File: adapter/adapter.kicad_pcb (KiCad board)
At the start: 2 copper layers, 16 parts, among them J1 MALE, J11 MALE, J12 FEMALE, J2 FEMALE, J3 USB_C_Receptacle_USB2.0, J5 DTR, U1 FT232RL

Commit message: Set design rules
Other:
- net class Default: clearance 0.2 -> 0.1524; trace_width 0.25 -> 0.1524; via_dia 0.8 -> 0.6; via_drill 0.4 -> 0.3
- rule trace_clearance: 0.2 -> 0.1524
- rule trace_min: 0.2 -> 0.1016
- rule via_min_size: 0.4 -> 0.5
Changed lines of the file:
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@@
   )
   (setup
-    (last_trace_width 0.25)
-    (trace_clearance 0.2)
+    (last_trace_width 0.1524)
+    (trace_clearance 0.1524)
     (zone_clearance 0.508)
     (zone_45_only no)
-    (trace_min 0.2)
-    (via_size 0.8)
-    (via_drill 0.4)
-    (via_min_size 0.4)
+    (trace_min 0.1016)
+    (via_size 0.6)
+    (via_drill 0.3)
+    (via_min_size 0.5)
     (via_min_drill 0.3)
+    (user_via 0.5 0.3)
     (uvia_size 0.3)
     (uvia_drill 0.1)
@@
   (net 30 "Net-(U1-Pad28)")
   (net_class Default "This is the default net class."
-    (clearance 0.2)
-    (trace_width 0.25)
-    (via_dia 0.8)
-    (via_drill 0.4)
+    (clearance 0.1524)
+    (trace_width 0.1524)
+    (via_dia 0.6)
+    (via_drill 0.3)
     (uvia_dia 0.3)
     (uvia_drill 0.1)

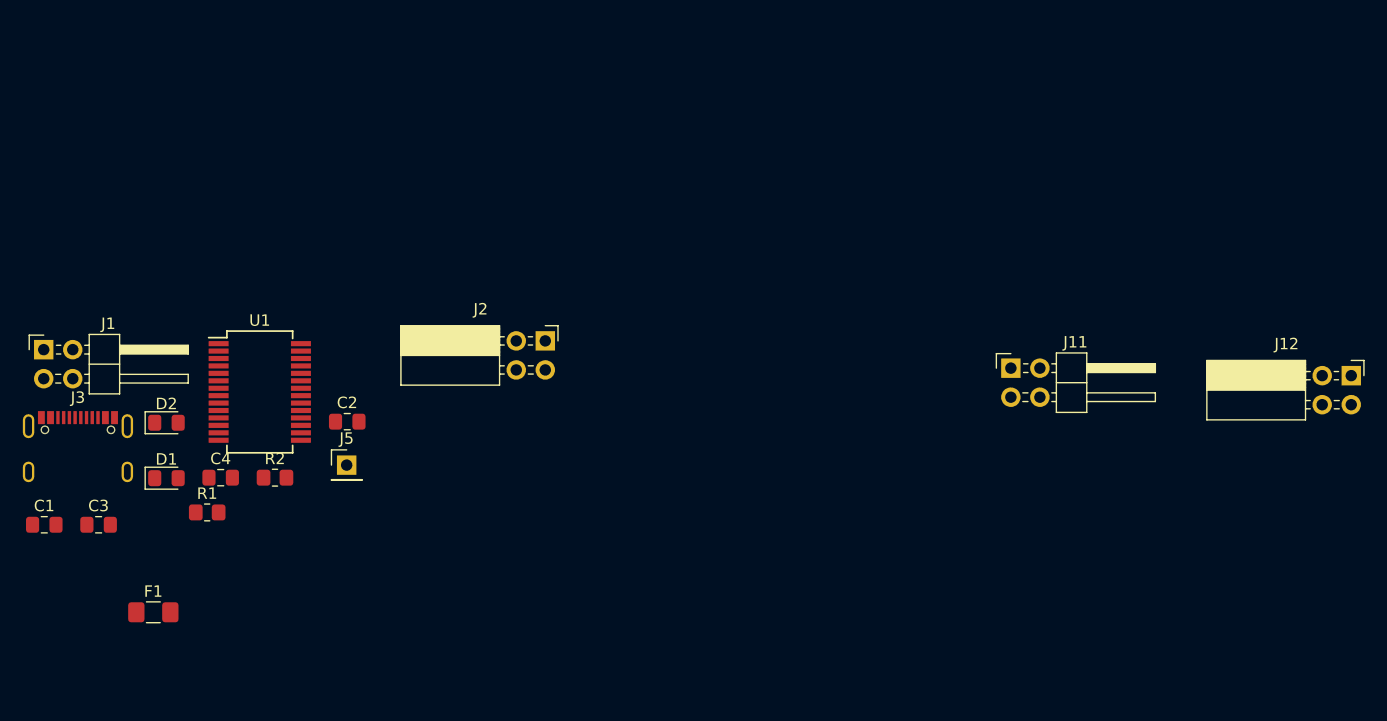
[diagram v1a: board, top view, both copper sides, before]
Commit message: Add holes for standoffs
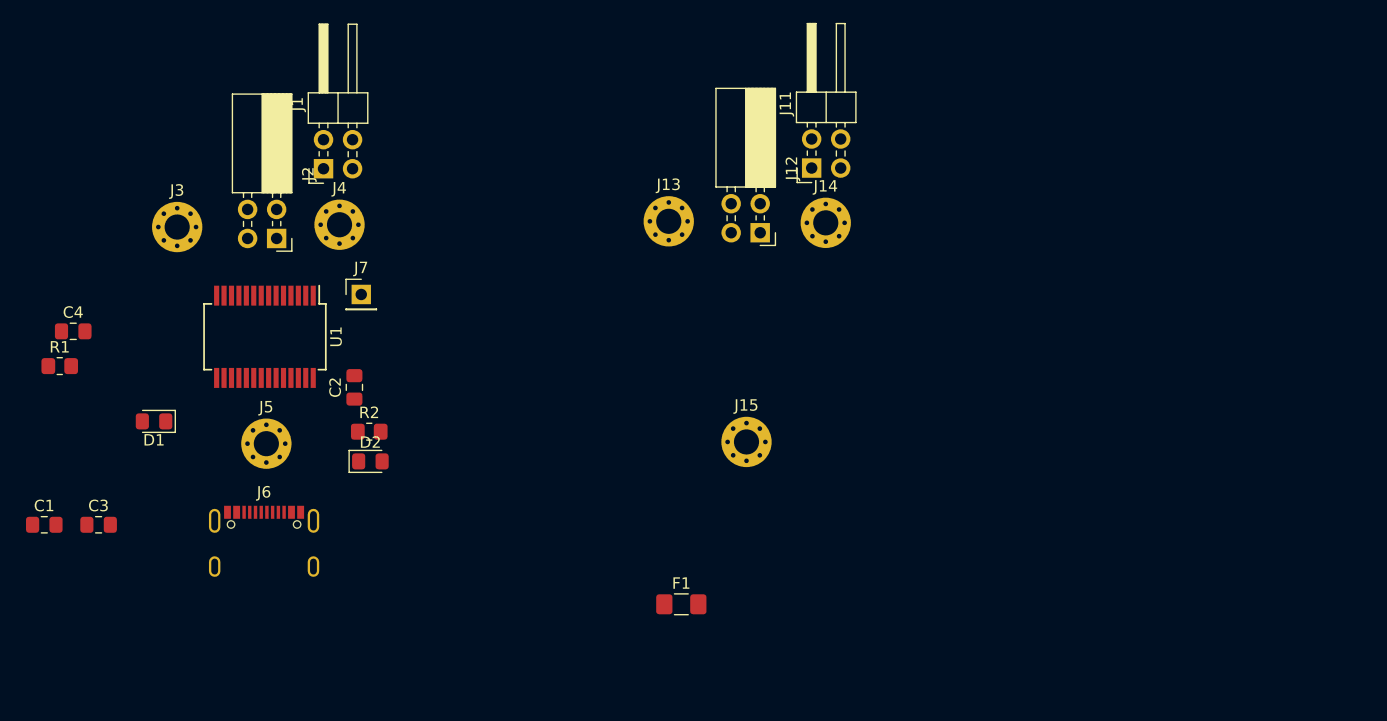
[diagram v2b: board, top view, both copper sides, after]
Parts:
- added J13: Conn_01x01, MountingHole:MountingHole_2.2mm_M2_Pad_Via, F.Cu at (144.0, 73.4)
- added J14: Conn_01x01, MountingHole:MountingHole_2.2mm_M2_Pad_Via, F.Cu at (157.7, 73.5)
- added J15: Conn_01x01, MountingHole:MountingHole_2.2mm_M2_Pad_Via, F.Cu at (150.8, 92.7)
- added J3: Conn_01x01, MountingHole:MountingHole_2.2mm_M2_Pad_Via, F.Cu at (101.0, 73.9)
- added J4: Conn_01x01, MountingHole:MountingHole_2.2mm_M2_Pad_Via, F.Cu at (115.2, 73.7)
- added J5: Conn_01x01, MountingHole:MountingHole_2.2mm_M2_Pad_Via, F.Cu at (108.8, 92.8)
- moved J12 53.2 mm to (152.0, 74.4), turned to 270 degrees
- moved F1 46.2 mm to (145.1, 106.9)
- moved J1 29.1 mm to (113.8, 68.8), turned to 90 degrees
- moved J2 25.2 mm to (109.7, 74.9), turned to 270 degrees
- moved J11 24.7 mm to (156.5, 68.7), turned to 90 degrees
- moved J6 18.3 mm to (108.6, 103.6)
- moved R1 18.2 mm to (90.7, 86.1)
- moved C4 18.2 mm to (91.9, 83.0)
- moved D2 18.2 mm to (117.9, 94.4)
- moved J7 15.0 mm to (117.1, 79.8)
- moved R2 9.18 mm to (117.8, 91.8)
- moved D1 5.09 mm to (99.0, 90.9), turned to 180 degrees
- moved U1 4.85 mm to (108.7, 83.5), turned to 270 degrees
- moved C2 3.06 mm to (116.5, 87.9), turned to 90 degrees
- renumbered J3 to J6, J5 to J7

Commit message: Add edge cuts and roughly place components
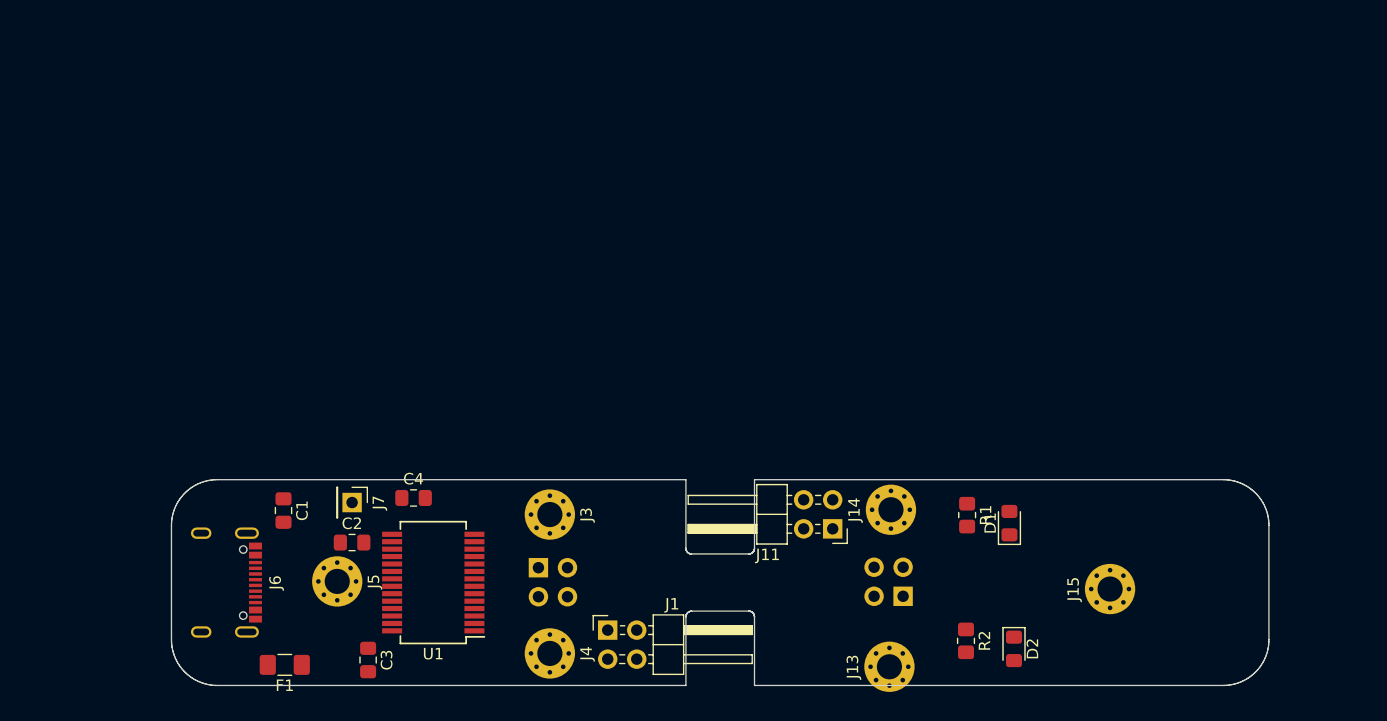
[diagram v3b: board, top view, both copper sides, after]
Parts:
- J12, J2: moved to B.Cu
- moved R1 80.4 mm to (170.1, 99.1), turned to 270 degrees
- moved D1 75.4 mm to (173.8, 99.8), turned to 90 degrees
- moved D2 58.6 mm to (174.2, 110.8), turned to 270 degrees
- moved R2 55.3 mm to (170.0, 110.1), turned to 270 degrees
- moved J1 47.4 mm to (138.7, 109.2), turned to 0 degrees
- moved J13 43.5 mm to (163.3, 112.4), turned to 90 degrees
- moved J4 41.8 mm to (133.6, 111.2), turned to 270 degrees
- moved J3 41.2 mm to (133.6, 99.0), turned to 270 degrees
- moved J2 36.8 mm to (132.6, 103.7), turned to 180 degrees
- moved F1 35.1 mm to (110.4, 112.2), turned to 180 degrees
- moved J15 34.3 mm to (182.6, 105.6), turned to 90 degrees
- moved J12 34.2 mm to (164.5, 106.2), turned to 0 degrees
- moved C4 33.1 mm to (121.7, 97.6)
- moved J11 31.6 mm to (158.3, 100.3), turned to 180 degrees
- moved C3 26.4 mm to (117.7, 111.8), turned to 270 degrees
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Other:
- board outline added: 96 x 18 mm

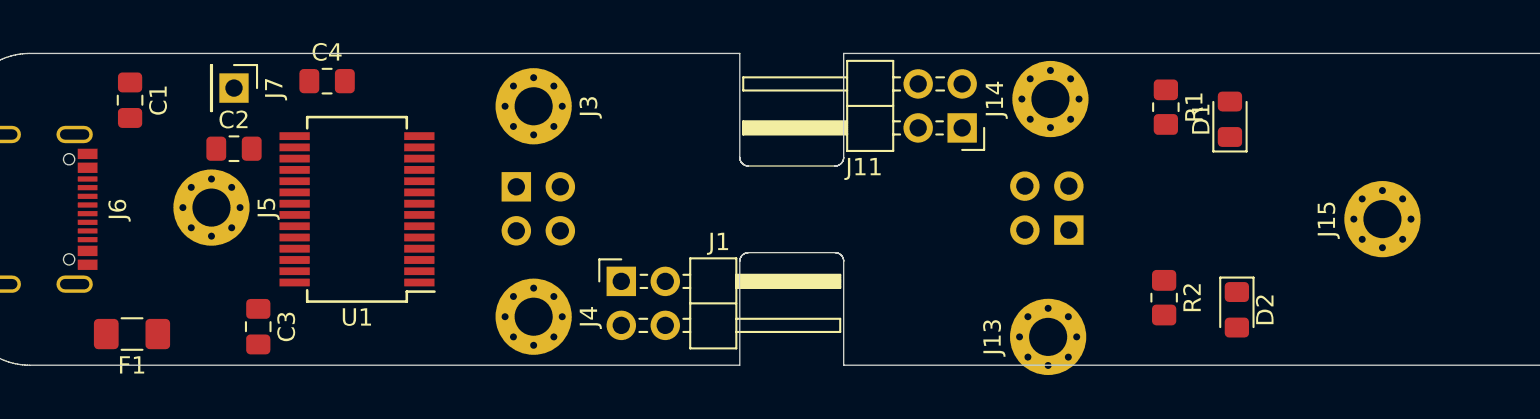
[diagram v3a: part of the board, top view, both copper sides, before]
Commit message: Position connectors and standoff holes
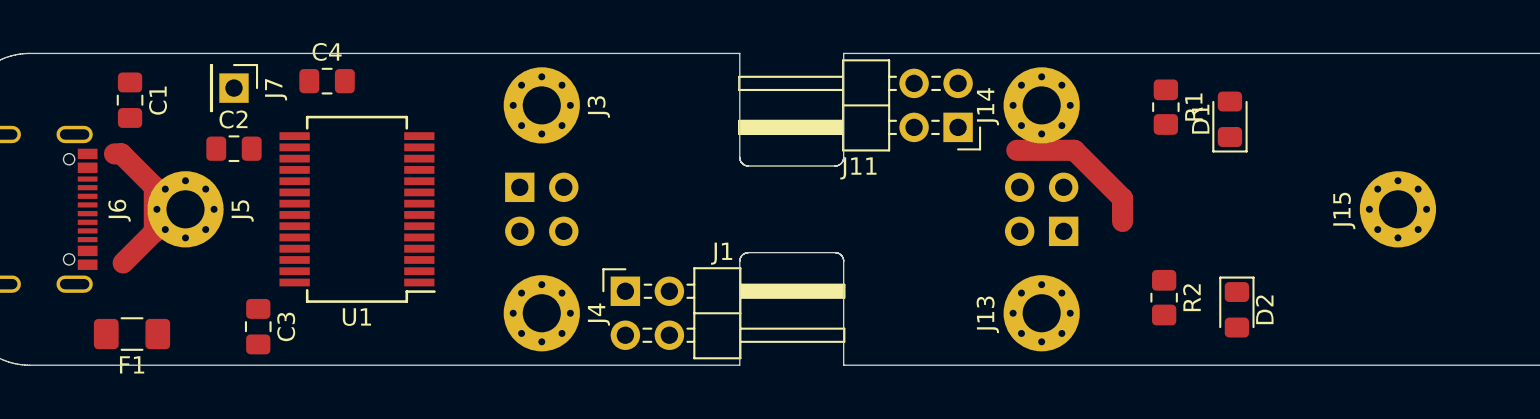
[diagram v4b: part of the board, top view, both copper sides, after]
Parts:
- moved J5 1.50 mm to (113.5, 105.0)
- moved J13 1.42 mm to (162.9, 111.0)
- moved J15 1.06 mm to (183.5, 105.0)
- moved J14 0.63 mm to (162.9, 99.0)
- moved J1 0.62 mm to (138.9, 109.7)
- moved J4 0.51 mm to (134.1, 111.0)
- moved J3 0.47 mm to (134.1, 99.0)
- moved J12 0.31 mm to (164.2, 106.3)
- moved J11 0.24 mm to (158.1, 100.3)
- moved J2 0.20 mm to (132.8, 103.7)
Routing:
- net (no net): track 0.00 -> 8.58 mm
- net Net-(J5-Pad1): track 0.00 -> 8.23 mm
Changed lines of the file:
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@@
     (thickness 1.6)
     (drawings 380)
-    (tracks 0)
+    (tracks 7)
     (zones 0)
     (modules 22)
@@
   )
   (setup
-    (last_trace_width 0.1524)
+    (last_trace_width 1.2192)
+    (user_trace_width 0.1524)
+    (user_trace_width 1.2192)
     (trace_clearance 0.1524)
     (zone_clearance 0.508)
@@
   )
   (module Connector_PinHeader_2.54mm:PinHeader_2x02_P2.54mm_Horizontal (layer F.Cu)
-    (at 138.66 109.16)
+    (at 138.896 109.73)
     (descr "Through hole angled pin header, 2x02, 2.54mm pitch, 6mm pin length, double rows")
     (tags "Through hole angled pin header THT 2x02 2.54mm double row")
@@
   )
   (module Connector_PinHeader_2.54mm:PinHeader_2x02_P2.54mm_Horizontal (layer F.Cu)
-    (at 158.34 100.3 180)
+    (at 158.104 100.27 180)
     (descr "Through hole angled pin header, 2x02, 2.54mm pitch, 6mm pin length, double rows")
     (tags "Through hole angled pin header THT 2x02 2.54mm double row")
@@
   )
   (module Connector_PinSocket_2.54mm:PinSocket_2x02_P2.54mm_Horizontal (layer B.Cu)
-    (at 132.6 103.7 180)
+    (at 132.8 103.73 180)
     (descr "Through hole angled socket strip, 2x02, 2.54mm pitch, 8.51mm socket length, double cols (from Kicad 4.0.7), script generated")
     (tags "Through hole angled socket strip THT 2x02 2.54mm double row")
@@
   )
   (module Connector_PinSocket_2.54mm:PinSocket_2x02_P2.54mm_Horizontal (layer B.Cu)
-    (at 164.5 106.2)
+    (at 164.2 106.27)
     (descr "Through hole angled socket strip, 2x02, 2.54mm pitch, 8.51mm socket length, double cols (from Kicad 4.0.7), script generated")
     (tags "Through hole angled socket strip THT 2x02 2.54mm double row")
@@
   )
   (module MountingHole:MountingHole_2.2mm_M2_Pad_Via (layer F.Cu)
-    (at 133.6 99.05 270)
+    (at 134.07 99 270)
     (descr "Mounting Hole 2.2mm, M2")
     (tags "mounting hole 2.2mm m2")
@@
   )
   (module MountingHole:MountingHole_2.2mm_M2_Pad_Via (layer F.Cu)
-    (at 133.6 111.2 270)
+    (at 134.07 111 270)
     (descr "Mounting Hole 2.2mm, M2")
     (tags "mounting hole 2.2mm m2")
@@
   )
   (module MountingHole:MountingHole_2.2mm_M2_Pad_Via (layer F.Cu)
-    (at 115 104.9 270)
+    (at 113.5 105 270)
     (descr "Mounting Hole 2.2mm, M2")
     (tags "mounting hole 2.2mm m2")
@@
   )
   (module MountingHole:MountingHole_2.2mm_M2_Pad_Via (layer F.Cu)
-    (at 163.302944 112.365685 90)
+    (at 162.93 111 90)
     (descr "Mounting Hole 2.2mm, M2")
     (tags "mounting hole 2.2mm m2")
@@
   )
   (module MountingHole:MountingHole_2.2mm_M2_Pad_Via (layer F.Cu)
-    (at 163.436218 98.632413 90)
+    (at 162.93 99 90)
     (descr "Mounting Hole 2.2mm, M2")
     (tags "mounting hole 2.2mm m2")
@@
   )
   (module MountingHole:MountingHole_2.2mm_M2_Pad_Via (layer F.Cu)
-    (at 182.602944 105.565687 90)
+    (at 183.5 105 90)
     (descr "Mounting Hole 2.2mm, M2")
     (tags "mounting hole 2.2mm m2")
@@
   (gr_line (start 146 102.5) (end 145.982929 102.499708) (layer Edge.Cuts) (width 0.05))
   (gr_line (start 151 102.5) (end 146 102.5) (layer Edge.Cuts) (width 0.05))
+  (segment (start 109.8 101.8) (end 111.7 103.7) (width 1.2192) (layer F.Cu) (net 29))
+  (segment (start 109.4 101.8) (end 109.8 101.8) (width 1.2192) (layer F.Cu) (net 29))
+  (segment (start 111.7 103.7) (end 111.7 106.3) (width 1.2192) (layer F.Cu) (net 29))
+  (segment (start 111.7 106.3) (end 109.9 108.1) (width 1.2192) (layer F.Cu) (net 29))
+  (segment (start 164.820176 101.594414) (end 161.494414 101.594414) (width 1.2192) (layer F.Cu) (net 0))
+  (segment (start 167.6 104.374238) (end 164.820176 101.594414) (width 1.2192) (layer F.Cu) (net 0))
+  (segment (start 167.6 105.7) (end 167.6 104.374238) (width 1.2192) (layer F.Cu) (net 0))
 )

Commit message: Update footprints
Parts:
- D1: value Red -> Green
- D2: value Green -> Red
- J13, J14, J15, J3, J4, J5: value Conn_01x01 -> STANDOFF
- moved R2 13.3 mm to (179.6, 100.8), turned to 0 degrees
- moved D2 9.86 mm to (174.8, 101.0), turned to 0 degrees
- moved R1 9.54 mm to (179.6, 97.9), turned to 0 degrees
- moved D1 2.14 mm to (174.8, 97.9), turned to 0 degrees
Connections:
- D1 pad 1: /Lower Board/TXLED -> Net-(D1-Pad1)
- D2 pad 1: /Lower Board/RXLED -> Net-(D2-Pad1)
- J13 pad 1: Net-(J13-Pad1) -> Net-(D1-Pad1)
- J14 pad 1: Net-(J14-Pad1) -> Net-(D2-Pad1)
- J3 pad 1: Net-(J3-Pad1) -> /Lower Board/TXLED
- J4 pad 1: Net-(J4-Pad1) -> /Lower Board/RXLED

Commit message: Add footprints for mouse bites
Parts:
- added H1: Mouse_bite, node:single_sided_tab_5mm, F.Cu at (145.5, 105.0)
- added H2: Mouse_bite, node:single_sided_tab_5mm, F.Cu at (151.5, 105.0)
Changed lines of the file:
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@@
     (tracks 7)
     (zones 0)
-    (modules 22)
+    (modules 24)
     (nets 35)
   )
@@
     )
   )
+  (module node:single_sided_tab_5mm (layer F.Cu)
+    (at 145.5 105 270)
+    (fp_text reference H1 (at 0 -2.5 90) (layer F.SilkS)
+      (effects (font (size 1 1) (thickness 0.15)))
+    )
+    (fp_text value Mouse_bite (at 0 3 90) (layer F.Fab)
+      (effects (font (size 1 1) (thickness 0.15)))
+    )
+    (fp_arc (start 3 -0.5) (end 2.5 -0.5) (angle -90) (layer Eco1.User) (width 0.05))
+    (fp_arc (start -3 -0.5) (end -3 0) (angle -90) (layer Eco1.User) (width 0.05))
+    (pad "" np_thru_hole circle (at 1.1 0.375 270) (size 0.6 0.6) (drill 0.6) (layers *.Cu *.Mask)
+      (clearance 0.2))
+    (pad "" np_thru_hole circle (at -2.2 0.375 270) (size 0.6 0.6) (drill 0.6) (layers *.Cu *.Mask)
+      (clearance 0.2))
+    (pad "" np_thru_hole circle (at -1.1 0.375 270) (size 0.6 0.6) (drill 0.6) (layers *.Cu *.Mask)
+      (clearance 0.2))
+    (pad "" np_thru_hole circle (at 0 0.375 270) (size 0.6 0.6) (drill 0.6) (layers *.Cu *.Mask)
+      (clearance 0.2))
+    (pad "" np_thru_hole circle (at 2.2 0.375 270) (size 0.6 0.6) (drill 0.6) (layers *.Cu *.Mask)
+      (clearance 0.2))
+  )
+  (module node:single_sided_tab_5mm (layer F.Cu)
+    (at 151.5 105 90)
+    (fp_text reference H2 (at 0 -2.5 90) (layer F.SilkS)
+      (effects (font (size 1 1) (thickness 0.15)))
+    )
+    (fp_text value Mouse_bite (at 0 3 90) (layer F.Fab)
+      (effects (font (size 1 1) (thickness 0.15)))
+    )
+    (fp_arc (start -3 -0.5) (end -3 0) (angle -90) (layer Eco1.User) (width 0.05))
+    (fp_arc (start 3 -0.5) (end 2.5 -0.5) (angle -90) (layer Eco1.User) (width 0.05))
+    (pad "" np_thru_hole circle (at 2.2 0.375 90) (size 0.6 0.6) (drill 0.6) (layers *.Cu *.Mask)
+      (clearance 0.2))
+    (pad "" np_thru_hole circle (at 0 0.375 90) (size 0.6 0.6) (drill 0.6) (layers *.Cu *.Mask)
+      (clearance 0.2))
+    (pad "" np_thru_hole circle (at -1.1 0.375 90) (size 0.6 0.6) (drill 0.6) (layers *.Cu *.Mask)
+      (clearance 0.2))
+    (pad "" np_thru_hole circle (at -2.2 0.375 90) (size 0.6 0.6) (drill 0.6) (layers *.Cu *.Mask)
+      (clearance 0.2))
+    (pad "" np_thru_hole circle (at 1.1 0.375 90) (size 0.6 0.6) (drill 0.6) (layers *.Cu *.Mask)
+      (clearance 0.2))
+  )
   (gr_line (start 151.01707 102.499708) (end 151 102.5) (layer Edge.Cuts) (width 0.05))
